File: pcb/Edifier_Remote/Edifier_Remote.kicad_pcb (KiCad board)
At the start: 2 copper layers, 33 x 70 mm, 9 parts, among them Q1 Q_NPN_BCE, U1 ESP32_DevKit

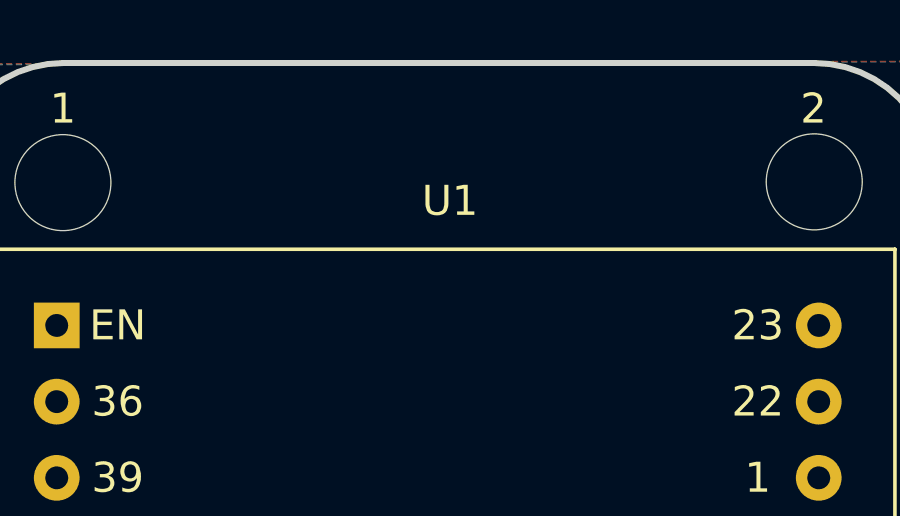
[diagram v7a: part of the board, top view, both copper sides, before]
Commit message: change pcb label
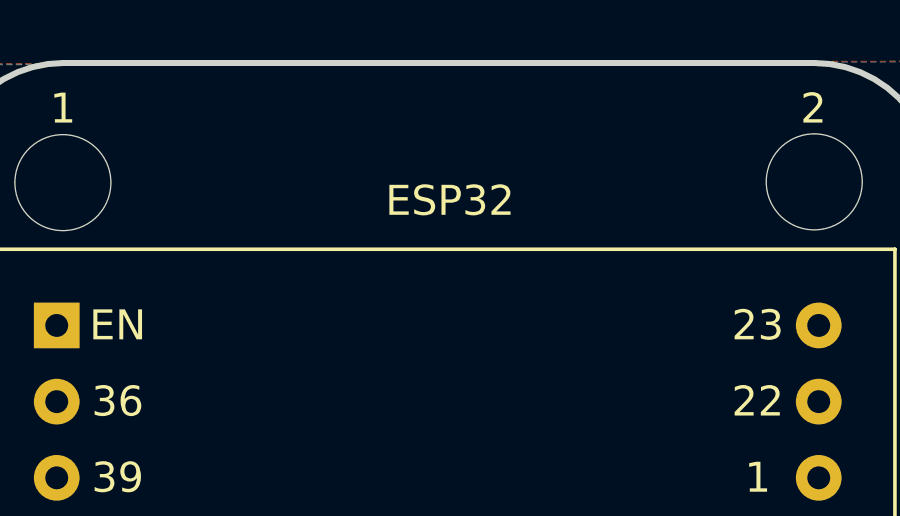
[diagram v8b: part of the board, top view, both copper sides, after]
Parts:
- renumbered U1 to ESP32
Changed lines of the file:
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@@
   (module ESP32:ESP32_DevKit_36PIN (layer F.Cu)
     (at 114.907 80.097)
-    (fp_text reference U1 (at 2.949 -9.231) (layer F.SilkS)
+    (fp_text reference ESP32 (at 2.949 -9.231) (layer F.SilkS)
       (effects (font (size 1 1) (thickness 0.15)))
     )
